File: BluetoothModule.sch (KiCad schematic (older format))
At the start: 13 parts, among them U1 BM83SM1-00TA

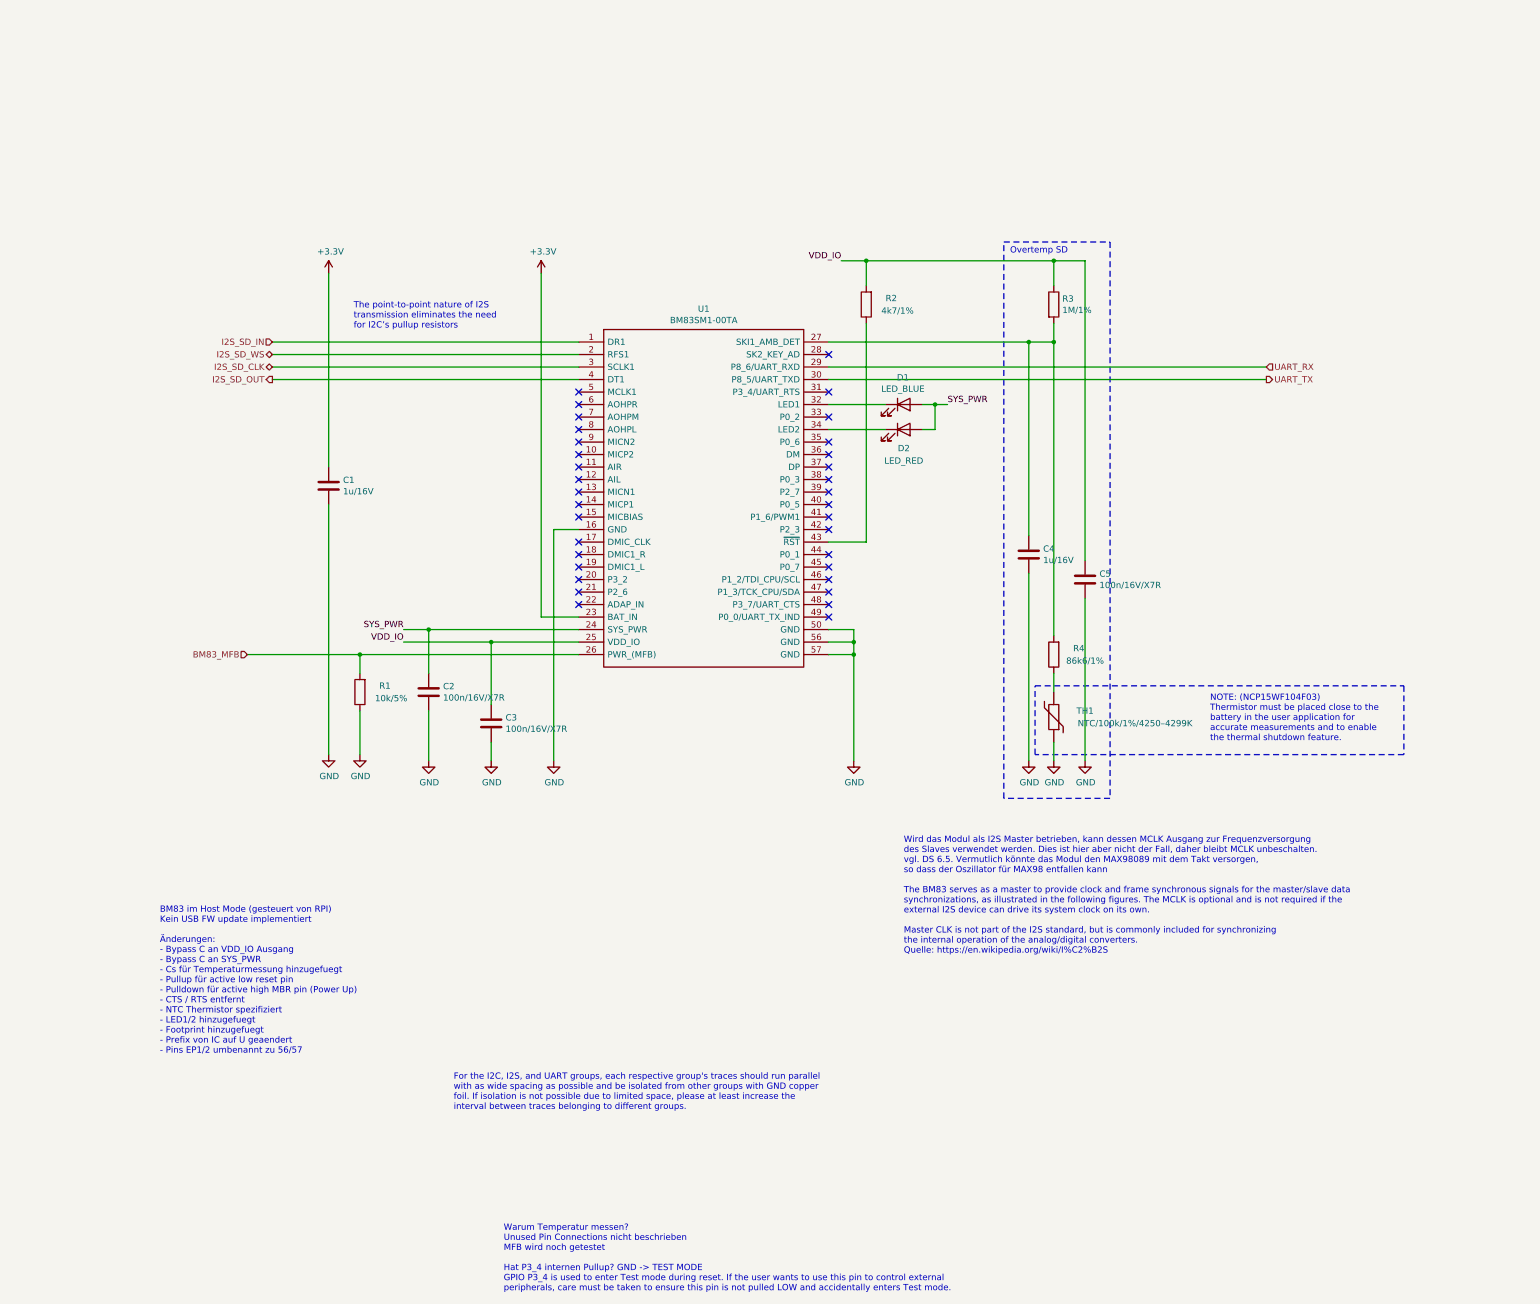
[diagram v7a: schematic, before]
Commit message: - CM4 update - Todo Liste auf Hauptschaltplan hinzugefügt
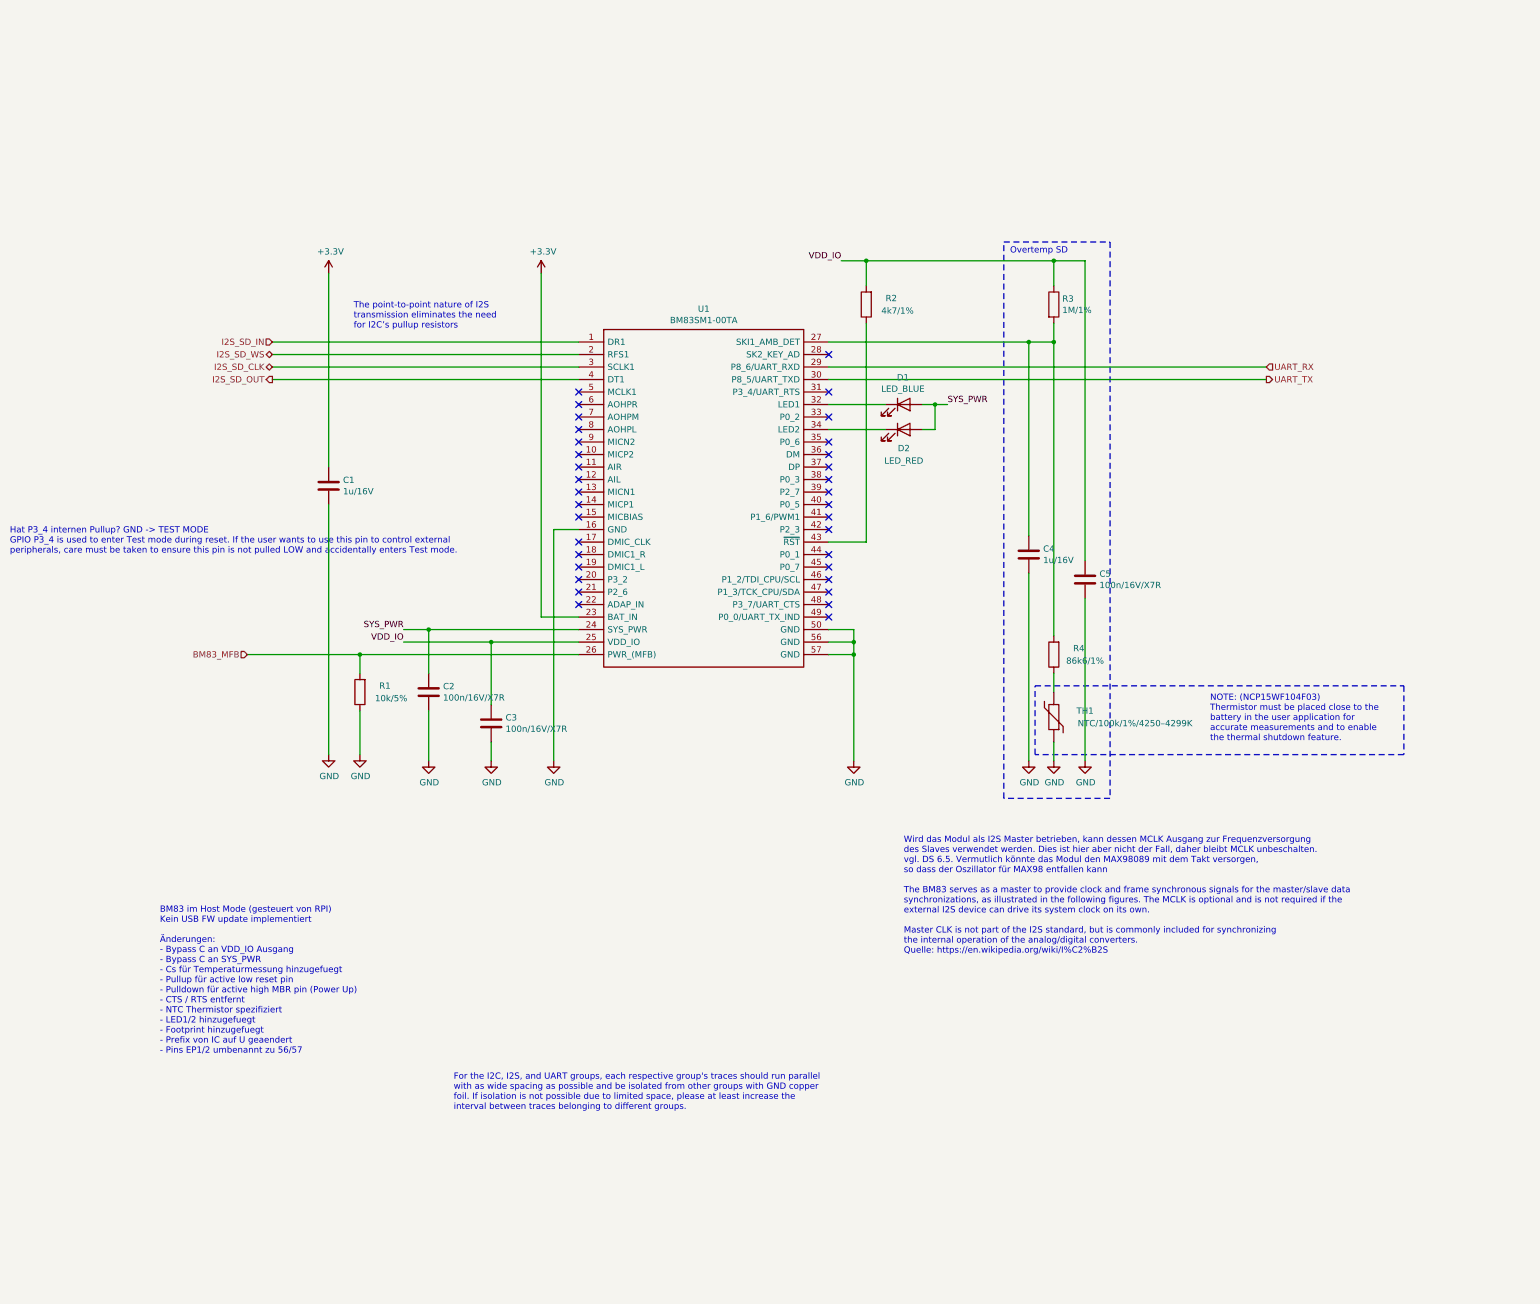
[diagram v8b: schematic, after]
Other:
- note added: "Hat P3_4 internen Pullup? GND -> TEST MODE\nGPIO P3_4 is used to enter Test mode during reset. If the user wants to use this pin to control external\nperipherals, care must be taken to ensure this pin is not pulled LOW and accidentally enters Test mode."
- note removed: "Warum Temperatur messen?\nUnused Pin Connections nicht beschrieben\nMFB wird noch getestet\n\nHat P3_4 internen Pullup? GND -> TEST MODE\nGPIO P3_4 is used to enter Test mode during reset. If the user wants to use this pin to control external\nperipherals, care must be taken to ensure this pin is not pulled LOW and accidentally enters Test mode."
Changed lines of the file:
@@
 NoConn ~ 6400 3550
 NoConn ~ 6400 1850
-Text Notes 3800 9050 0    50   ~ 0
-Warum Temperatur messen?\nUnused Pin Connections nicht beschrieben\nMFB wird noch getestet\n\nHat P3_4 internen Pullup? GND -> TEST MODE\nGPIO P3_4 is used to enter Test mode during reset. If the user wants to use this pin to control external\nperipherals, care must be taken to ensure this pin is not pulled LOW and accidentally enters Test mode.
+Text Notes -150 3150 0    50   ~ 0
+Hat P3_4 internen Pullup? GND -> TEST MODE\nGPIO P3_4 is used to enter Test mode during reset. If the user wants to use this pin to control external\nperipherals, care must be taken to ensure this pin is not pulled LOW and accidentally enters Test mode.
 Wire Wire Line
 	3000 3750 3200 3750
